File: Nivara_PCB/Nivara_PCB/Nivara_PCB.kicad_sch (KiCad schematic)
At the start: 26 parts, among them CN1 ANALOG_IN, CN2 RELAY, J1 AUXILIAR, P1 NPN_IN, P2 PNP_IN, P3 D_IN, P4 RUN/STOP, P5 NPN_OUT, P6 PNP_OUT, P7 RS485, P8 ANALOG_OUT., U1 2.54-2*2, U2 FUENTE IN, U20 FUENTE EX

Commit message: Terminaciones de diseño.
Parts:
- removed F1: BSMD1812-150-33V, EasyEDA:F1812, symbol EasyEDA:BSMD1812-150-33V
- added U21: ~, EasyEDA:Reseatteble Fuse, symbol EasyEda:Reseatteble_Fuse
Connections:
- net VCC: now also U21.2
- net VIN: now also U21.1
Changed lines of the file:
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@@
-	)
-	(symbol
-		(lib_id "EasyEDA:BSMD1812-150-33V")
-		(at 201.93 66.04 0)
-		(unit 1)
-		(exclude_from_sim no)
-		(in_bom yes)
-		(on_board yes)
-		(dnp no)
-		(fields_autoplaced yes)
-		(property "Reference" "F1"
-			(at 203.2 60.96 0)
-			(effects
-				(font
-					(size 1.27 1.27)
-				)
-			)
-		)
-		(property "Value" "BSMD1812-150-33V"
-			(at 203.2 63.5 0)
-			(effects
-				(font
-					(size 1.27 1.27)
-				)
-			)
-		)
-		(property "Footprint" "EasyEDA:F1812"
-			(at 201.93 73.66 0)
-			(effects
-				(font
-					(size 1.27 1.27)
-				)
-				(hide yes)
-			)
-		)
-		(property "Datasheet" "https://lcsc.com/product-detail/PTC-Resettable-Fuses_BHFUSE-BSMD1812-150-33V_C883154.html"
-			(at 201.93 76.2 0)
-			(effects
-				(font
-					(size 1.27 1.27)
-				)
-				(hide yes)
-			)
-		)
-		(property "Description" ""
-			(at 201.93 66.04 0)
-			(effects
-				(font
-					(size 1.27 1.27)
-				)
-				(hide yes)
-			)
-		)
-		(property "LCSC Part" "C883154"
-			(at 201.93 78.74 0)
-			(effects
-				(font
-					(size 1.27 1.27)
-				)
-				(hide yes)
-			)
-		)
-		(pin "1"
-		)
-		(pin "2"
-		)
-		(instances
-			(project ""
-				(path "/13184db0-a71d-4054-b13a-bbf46d2b100d"
-					(reference "F1")
-					(unit 1)
-				)
-			)
-		)
 	)
 	(symbol
@@
 					(unit 1)
 				)
+			)
+		)
+	)
+	(symbol
+		(lib_id "EasyEda:Reseatteble_Fuse")
+		(at 203.2 66.04 0)
+		(unit 1)
+		(exclude_from_sim no)
+		(in_bom yes)
+		(on_board yes)
+		(dnp no)
+		(fields_autoplaced yes)
+		(property "Reference" "U21"
+			(at 203.2 59.69 0)
+			(effects
+				(font
+					(size 1.27 1.27)
+				)
+			)
+		)
+		(property "Value" "~"
+			(at 203.2 62.23 0)
+			(effects
+				(font
+					(size 1.27 1.27)
+				)
+			)
+		)
+		(property "Footprint" "EasyEDA:Reseatteble Fuse"
+			(at 203.2 66.04 0)
+			(effects
+				(font
+					(size 1.27 1.27)
+				)
+				(hide yes)
+			)
+		)
+		(property "Datasheet" ""
+			(at 203.2 66.04 0)
+			(effects
+				(font
+					(size 1.27 1.27)
+				)
+				(hide yes)
+			)
+		)
+		(property "Description" ""
+			(at 203.2 66.04 0)
+			(effects
+				(font
+					(size 1.27 1.27)
+				)
+				(hide yes)
+			)
+		)
+		(pin "1"
+		)
+		(pin "2"
+		)
+		(instances
+			(project ""
+				(path "/13184db0-a71d-4054-b13a-bbf46d2b100d"
+					(reference "U21")
+					(unit 1)
+				)

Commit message: TERMINACIONES Y AJUSTES FINALES
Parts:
- removed AE1: Antenna, symbol EasyEDA:Antenna
- removed C1: 100nF, PCM_Capacitor_SMD_AKL:C_0603_1608Metric, symbol EasyEDA:C_0603
- removed CN1: ANALOG_IN, EasyEDA:CONN-TH_DB128V-5.0-4P, symbol EasyEDA:DB128V-5.08-4P-GN-S
- removed CN2: RELAY, EasyEDA:CONN-TH_DB126V-5.0-6P-GN, symbol EasyEDA:DB128V-5.08-6P-GN-S
- removed D1: SS12, PCM_Diode_SMD_AKL:D_SMA, symbol EasyEDA:SS12
- removed D2: SM712, PCM_Package_TO_SOT_SMD_AKL:SOT-23, symbol EasyEDA:SM712
- removed J1: AUXILIAR, Connector_PinSocket_2.54mm:PinSocket_1x02_P2.54mm_Vertical, symbol EasyEDA:PINHD_1x2_Female
- removed P1: NPN_IN, EasyEDA:CONN-TH_XY126V-5.0-2P, symbol EasyEDA:WJ500V-5.08-2P-14-00A
- removed P2: PNP_IN, EasyEDA:CONN-TH_XY126V-5.0-2P, symbol EasyEDA:WJ500V-5.08-2P-14-00A
- removed P3: D_IN, EasyEDA:CONN-TH_XY126V-5.0-2P, symbol EasyEDA:WJ500V-5.08-2P-14-00A
- removed P4: RUN/STOP, EasyEDA:CONN-TH_XY126V-5.0-2P, symbol EasyEDA:WJ500V-5.08-2P-14-00A
- removed P5: NPN_OUT, EasyEDA:CONN-TH_XY126V-5.0-2P, symbol EasyEDA:WJ500V-5.08-2P-14-00A
- removed P6: PNP_OUT, EasyEDA:CONN-TH_XY126V-5.0-2P, symbol EasyEDA:WJ500V-5.08-2P-14-00A
- removed P7: RS485, EasyEDA:CONN-TH_3P-P5.00_WJ500V-5.08-3P, symbol EasyEDA:WJ500V-5.08-3P-14-00A
- removed P8: ANALOG_OUT., EasyEDA:CONN-TH_3P-P5.00_WJ500V-5.08-3P, symbol EasyEDA:WJ500V-5.08-3P-14-00A
- removed R56, R57: 33, PCM_Resistor_SMD_AKL:R_0603_1608Metric, symbol EasyEda:R_0603
- removed U1: 2.54-2*2, Connector_PinSocket_2.54mm:PinSocket_2x02_P2.54mm_Vertical, symbol EasyEda:2.54-2*2
- removed U2: FUENTE IN, EasyEDA:CONN-TH_XY126V-5.0-2P, symbol EasyEDA:XY126V-5.0-2P
- removed U20: FUENTE EX, EasyEDA:CONN-TH_XY126V-5.0-2P, symbol EasyEDA:XY126V-5.0-2P
- added D1: LED_USB, LED_SMD:LED_0603_1608Metric, symbol EasyEDA:LED
- added J10, J11, J13, J3, J5, J6, J7, J8: Bolnera 2P, TerminalBlock_Phoenix:TerminalBlock_Phoenix_MKDS-1,5-2-5.08_1x02_P5.08mm_Horizontal, symbol Connector:Screw_Terminal_01x02
- added J12: Bolnera 4P, TerminalBlock_Phoenix:TerminalBlock_Phoenix_MKDS-1,5-4-5.08_1x04_P5.08mm_Horizontal, symbol Connector:Screw_Terminal_01x04
- added J14: Bolnera 6P, TerminalBlock_Phoenix:TerminalBlock_Phoenix_MKDS-1,5-6-5.08_1x06_P5.08mm_Horizontal, symbol Connector:Screw_Terminal_01x06
- added J15: PINHD_2x2_Male, Connector_PinHeader_2.54mm:PinHeader_2x02_P2.54mm_Vertical, symbol PCM_SL_Pin_Headers:PINHD_2x2_Male
- added J2: Auxiliares, Connector_PinHeader_2.54mm:PinHeader_1x02_P2.54mm_Vertical, symbol Connector:Conn_01x02_Pin
- added J4, J9: Bolnera 3P, TerminalBlock_Phoenix:TerminalBlock_Phoenix_MKDS-1,5-3-5.08_1x03_P5.08mm_Horizontal, symbol Connector:Screw_Terminal_01x03
- added R65, R67: 5.1K, PCM_Resistor_SMD_AKL:R_0603_1608Metric, symbol EasyEDA:R_0603
- added R66: 500, PCM_Resistor_SMD_AKL:R_0603_1608Metric, symbol EasyEDA:R_0603
- added U1: GT-USB-7010ASV, EasyEDA:USB-C-SMD_G-SWITCH_GT-USB-7010ASV, symbol EasyEDA:GT-USB-7010ASV
- D3: LCSC Part (none) -> C148231; Part # (none) -> SMAJ33A
- D4: renamed from D33; LCSC Part (none) -> C148231; Part # (none) -> SMAJ33A
- F1: renamed from F2; Part # (none) -> BSMD1812-150-33V
- F3: renamed from U21; value ~ -> Resettable fuse; LCSC Part (none) -> C7433877; Part # (none) -> BSMD1812-200-33V
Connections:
- net D+: now also J15.3, U1.A6 (DP1), U1.B6 (DP2)
- net Earth: now also J11.2 (Pin_2), J13.2 (Pin_2)
- net GND: now also J10.2 (Pin_2), J12.4 (Pin_4), J4.3 (Pin_3), J9.3 (Pin_3)
- net NIVARA_BOARD/A0_10_IN_1: now also J12.2 (Pin_2)
- net NIVARA_BOARD/A0_32_IN_1: now also J12.3 (Pin_3)
- net NIVARA_BOARD/A0_V_OUT_1: now also J9.1 (Pin_1)
- net NIVARA_BOARD/A4_20_IN_1: now also J12.1 (Pin_1)
- net NIVARA_BOARD/AUX_1: now also J2.1 (Pin_1)
- net NIVARA_BOARD/AUX_2: now also J2.2 (Pin_2)
- net NIVARA_BOARD/D_IN_1: now also J6.1 (Pin_1)
- net NIVARA_BOARD/D_IN_2: now also J6.2 (Pin_2)
- net NIVARA_BOARD/I_OUT: now also J9.2 (Pin_2)
- net NIVARA_BOARD/NPN_IN_1: now also J3.1 (Pin_1)
- net NIVARA_BOARD/NPN_IN_2: now also J3.2 (Pin_2)
- net NIVARA_BOARD/NPN_OUT_1: now also J7.1 (Pin_1)
- net NIVARA_BOARD/NPN_OUT_2: now also J7.2 (Pin_2)
- net NIVARA_BOARD/PNP_IN_1: now also J5.1 (Pin_1)
- net NIVARA_BOARD/PNP_IN_2: now also J5.2 (Pin_2)
- net NIVARA_BOARD/PNP_OUT_1: now also J8.1 (Pin_1)
- net NIVARA_BOARD/PNP_OUT_2: now also J8.2 (Pin_2)
- net NIVARA_BOARD/RLY_1_C: now also J14.2 (Pin_2)
- net NIVARA_BOARD/RLY_1_NC: now also J14.1 (Pin_1)
- net NIVARA_BOARD/RLY_1_NO: now also J14.3 (Pin_3)
- net NIVARA_BOARD/RLY_2_C: now also J14.5 (Pin_5)
- net NIVARA_BOARD/RLY_2_NC: now also J14.4 (Pin_4)
- net NIVARA_BOARD/RLY_2_NO: now also J14.6 (Pin_6)
- net NIVARA_BOARD/RS485_A+: now also J4.1 (Pin_1)
- net NIVARA_BOARD/RS485_B-: now also J4.2 (Pin_2)
- net NIVARA_BOARD/RUN/STOP: now also J13.1 (Pin_1)
- net VIN: now also J10.1 (Pin_1)
- net at F1.1: now also J11.1 (Pin_1)
- new net: D1.1 (K), R66.2
- new net: R65.2, U1.A5 (CC1)
- new net: J15.1, U1.A7 (DN1), U1.B7 (DN2)
- new net: R67.2, U1.B5 (CC2)
- new net +5V: D1.2 (A), J15.2, U1.A4B9 (VBUS), U1.B4A9 (VBUS)
- new net GND1: J15.4, R65.1, R66.1, R67.1, U1.1 (SHELL), U1.2 (SHELL), U1.3 (SHELL), U1.4 (SHELL), U1.A1B12 (GND), U1.B1A12 (GND)
- no-connect marks 0 -> 1
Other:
- added sheet USB (USB.kicad_sch)

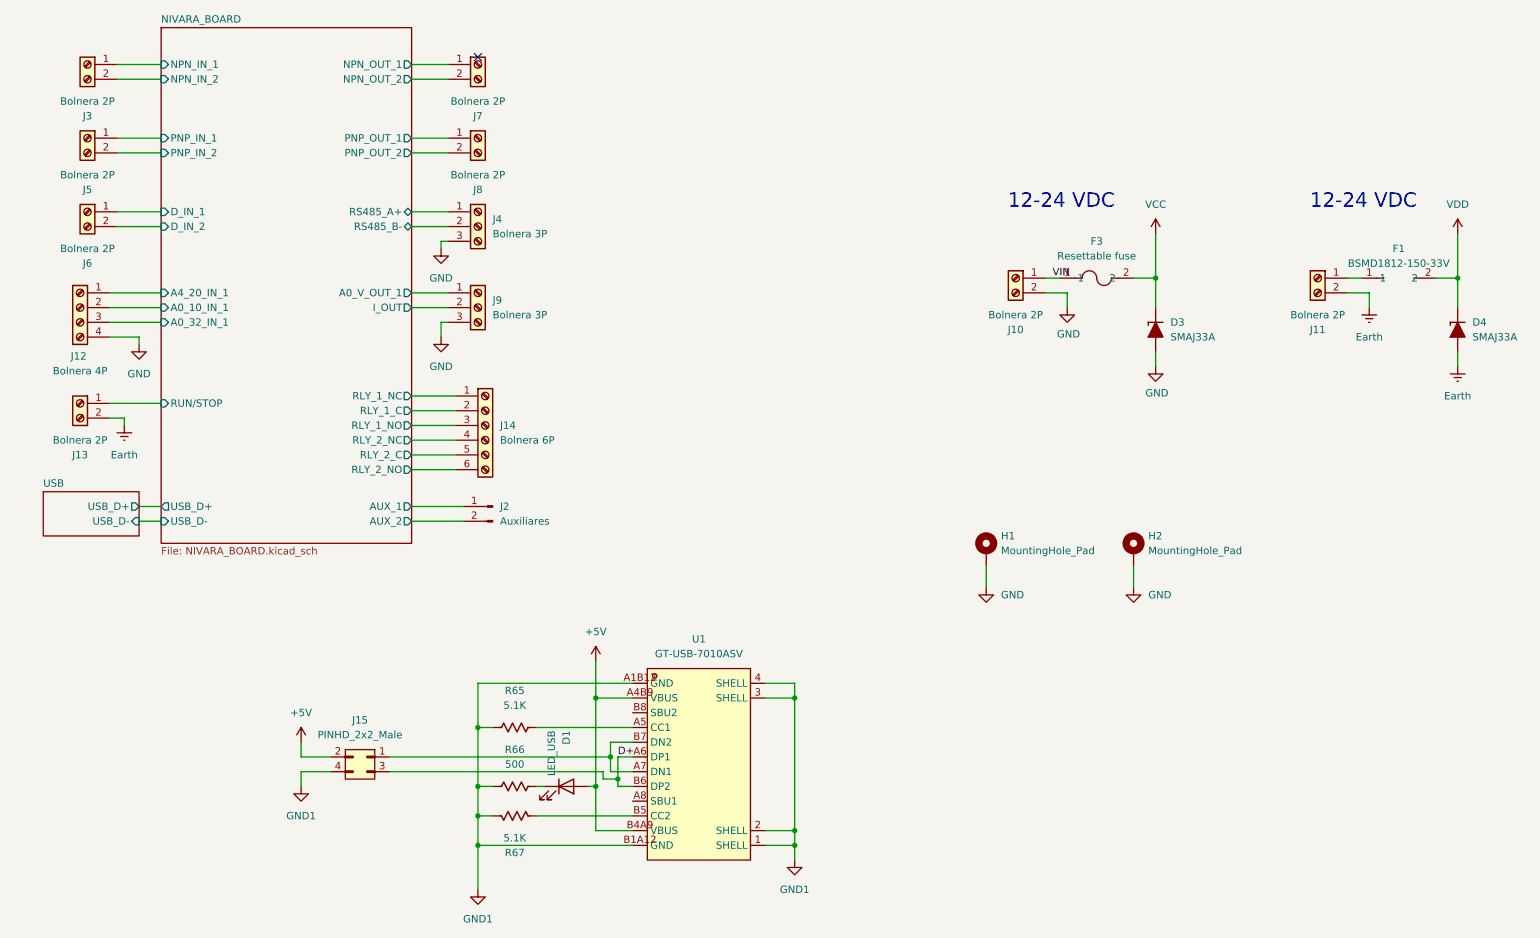
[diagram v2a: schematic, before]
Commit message: Cambios en las silscreen de los componentes.
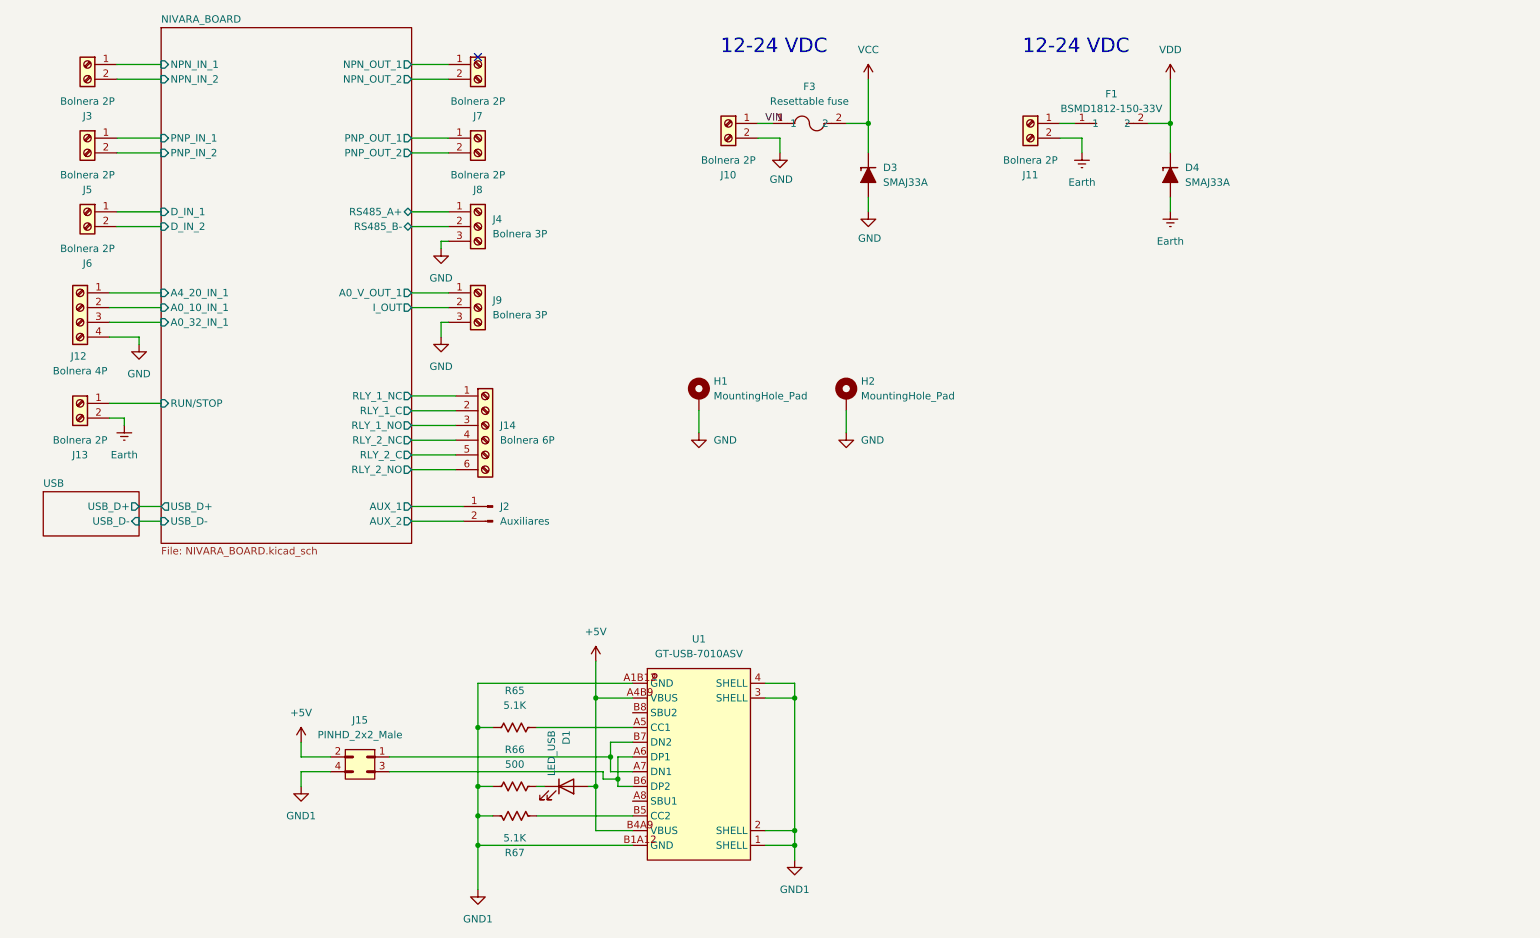
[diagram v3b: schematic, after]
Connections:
- net D+: no longer names the net of J15.3, U1.A6 (DP1), U1.B6 (DP2)
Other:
- moved on the sheet: D3, D4, F1, F3, H1, H2, J10, J11
